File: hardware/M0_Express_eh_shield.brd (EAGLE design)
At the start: 51.3 x 53.3 mm, 30 parts, among them U1 TLV3691, U2 AB0815, U3 Value, U4 MIC841, U5 TPS781, X2 ABS05-32.768KHZ-9-T

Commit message: updates and programmer
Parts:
- removed JP11: (no value), SparkFun-Connectors:1X06-1.27MM
- added JP2: (no value), SparkFun-Connectors:2X5_1.27MM
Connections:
- net GND: now also JP2.10, JP2.9; no longer JP11.1
- net MSP430_RST: now also JP2.5, JP2.6; no longer JP11.3
- net MSP430_TEST: now also JP2.3, JP2.4; no longer JP11.2
- net RX_DEBUG: now also JP2.2; no longer JP11.4
- net TX_DEBUG: now also JP2.7, JP2.8; no longer JP11.5
- net VCC: now also JP2.1; no longer JP11.6

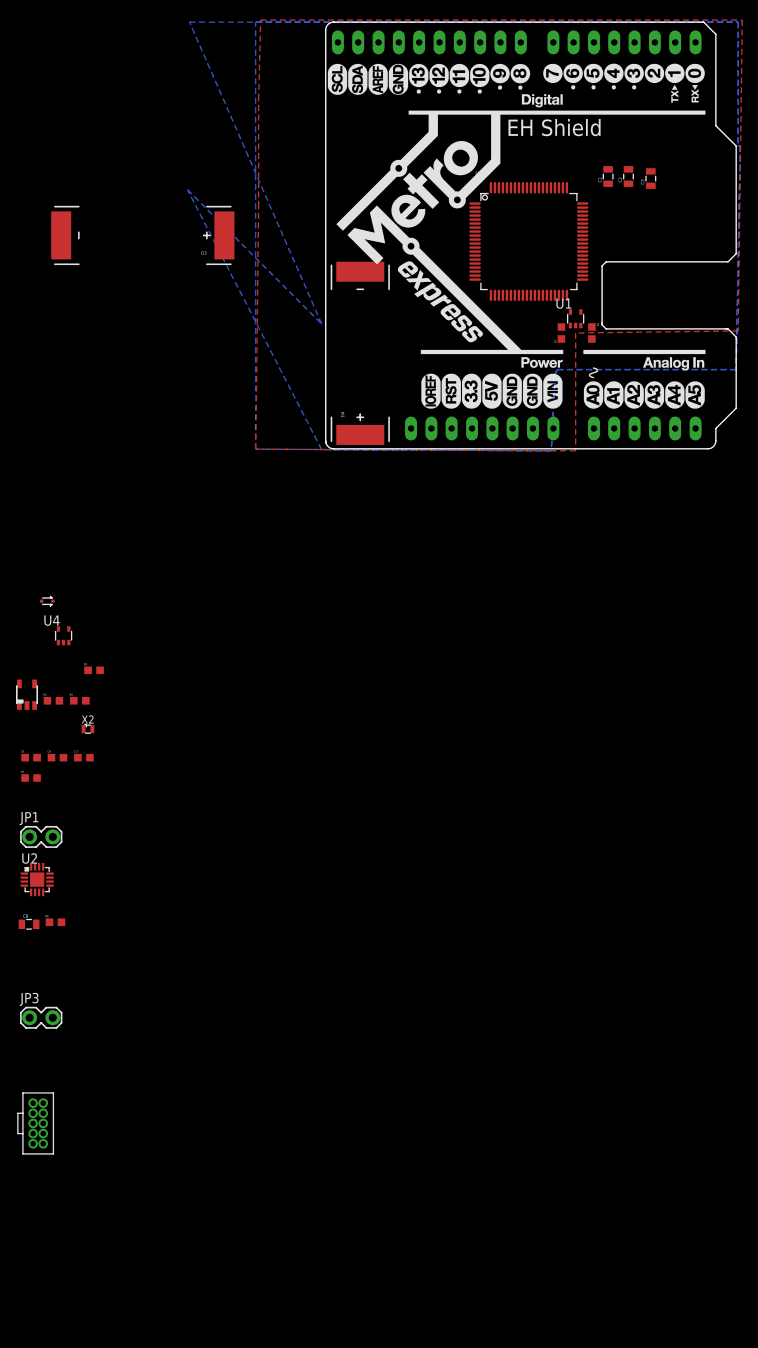
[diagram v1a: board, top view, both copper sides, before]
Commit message: finished schematic, basic board layout, need to route and order
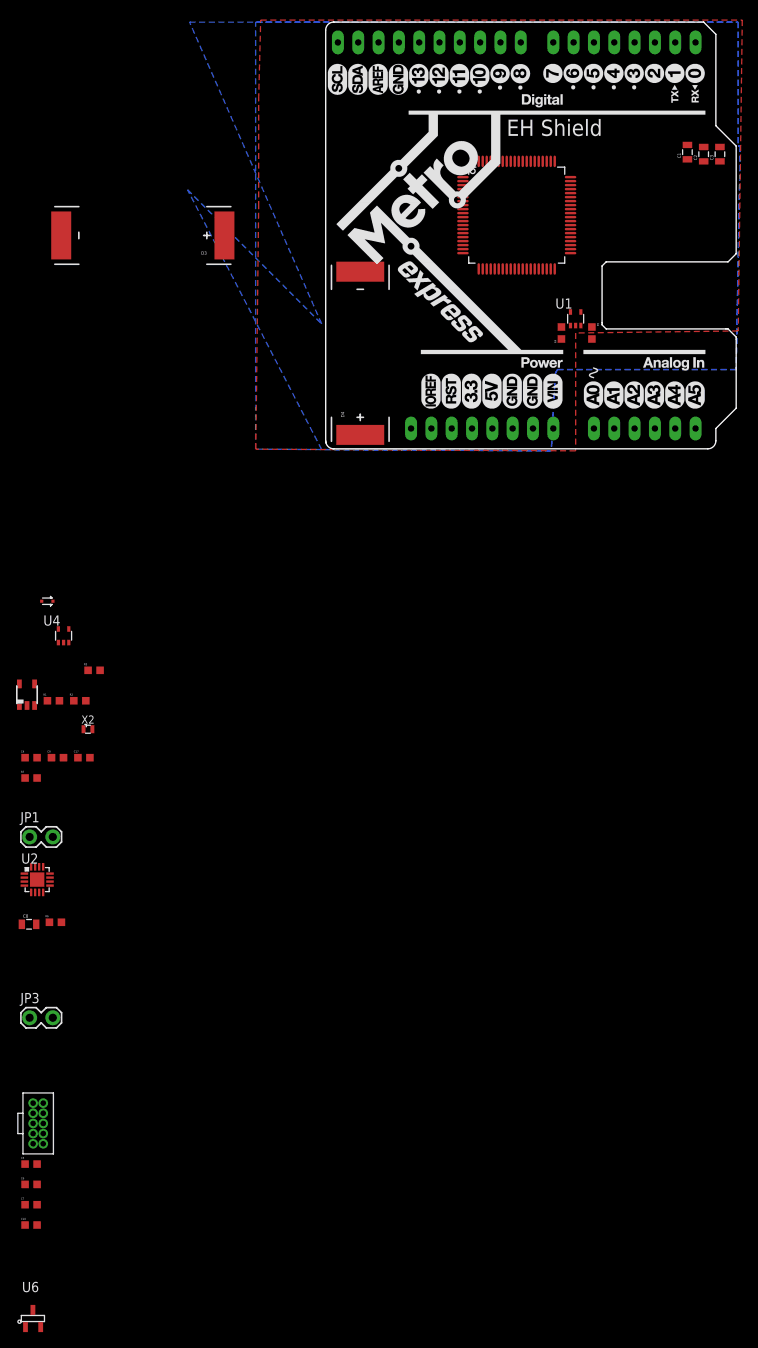
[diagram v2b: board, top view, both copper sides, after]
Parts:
- added C10, C5, C6, C7: 0.1u, tiny_passives:0603
- added U6: ISL21080, isl21080:SOT-23
- R1: value 2.2M -> 695k
- R2: value 2.2M -> 617k
- R3: value 1.3M -> 688k
- R4: value 1.05M -> 2.2M
- R5: value 649k -> 2.9M
- moved R2 78.8 mm to (-13.5, -31.5), turned to 0 degrees
- moved R5 78.8 mm to (50.5, 14.5), turned to 270 degrees
- moved R1 78.4 mm to (-16.8, -31.5), turned to 0 degrees
- moved R4 78.4 mm to (46.7, 14.5), turned to 90 degrees
- moved C1 10.4 mm to (62.5, 37.1)
- moved C2 9.80 mm to (64.5, 36.8)
- moved C3 9.16 mm to (66.5, 36.8)
- moved U3 3.64 mm to (41.1, 29.2)
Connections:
- removed net A4: AD.5
- removed net A5: AD.6
- new net VREF: U1.3, U6.2
- net GND: now also C10.2, C5.2, C6.2, C7.2, R5.1, U6.3; no longer R2.1, U1.3
- net N$2: now also R1.1, R2.1; no longer R4.1, R5.1
- net N$3: now also R2.2; no longer R5.2
- net N$7: now also C6.1
- net PFAIL: now also AD.5
- net VCAP_HALF: now also AD.6, R4.1, R5.2; no longer R1.1, R2.2
- net VCC: now also C10.1, C5.1, C7.1, U6.1

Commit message: finished hardware
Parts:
- removed C1, C3: (no value), SparkFun-Capacitors:0805
- added C11: 0.1u, tiny_passives:0603
- added JP4: (no value), SparkFun-Connectors:SCREWTERMINAL-5MM-2
- C2: value (none) -> 10u
- D1: value RB751 -> BAT20JFILM; device SparkFun-DiscreteSemi:SOD-523 -> SparkFun-DiscreteSemi:SOD-323
- moved U6 154.6 mm to (14.7, 42.1), turned to 90 degrees
- moved C10 144.7 mm to (25.8, 40.3), turned to 270 degrees
- moved C6 143.1 mm to (31.0, 41.9), turned to 90 degrees
- moved JP3 129.0 mm to (44.5, 40.9), turned to 90 degrees
- moved C5 128.9 mm to (3.81, 37.3), turned to 180 degrees
- moved C7 123.9 mm to (18.6, 23.4), turned to 270 degrees
- moved JP2 118.9 mm to (24.6, 28.8), turned to 180 degrees
- moved JP1 111.6 mm to (47.2, 40.9), turned to 90 degrees
- moved R7 89.7 mm to (22.3, 38.3), turned to 90 degrees
- moved R2 89.6 mm to (34.8, 43.9)
- moved R1 88.4 mm to (32.5, 41.9), turned to 270 degrees
- moved D1 88.3 mm to (41.4, 46.7)
- moved C4 88.3 mm to (24.0, 38.2), turned to 90 degrees
- moved U5 87.5 mm to (28.1, 42.3)
- moved R3 86.0 mm to (37.3, 42.9), turned to 90 degrees
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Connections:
- removed net D6: IOL.2
- removed net D7: IOL.1
- net GND: now also C11.2, JP4.2; no longer C1.2, C3.2
- net NV_READ: now also IOL.1, U3.51; no longer IOH.10, U3.52
- net NV_WRITE: now also U3.52; no longer U3.51
- net PFAIL: now also IOL.2, U3.41; no longer AD.5, U3.2
- net REG_SET: now also U3.50; no longer U3.3
- net RTC_CE: now also U3.7; no longer U3.26
- net RTC_SCLK: now also U3.10; no longer U3.25
- net RTC_SIMO: now also U3.8; no longer U3.13
- net RTC_SOMI: now also U3.9; no longer U3.14
- net RX_DEBUG: now also U3.36; no longer U3.42
- net TX_DEBUG: now also U3.35; no longer U3.41
- net VCAP: now also JP4.1; no longer C1.1, C3.1
- net VCAP_HALF: now also IOH.10, U3.27; no longer AD.6, U3.1
- net VCC: now also C11.1
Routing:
- net VCAP: track 0.00 -> 62.9 mm, vias 0 -> 2
- net PFAIL: track 0.00 -> 30.7 mm, vias 0 -> 1
- net VCAP_HALF: track 0.00 -> 28.8 mm, vias 0 -> 2
- net NV_READ: track 0.00 -> 26.5 mm, vias 0 -> 1
- net REG_SET: track 0.00 -> 23.7 mm, vias 0 -> 2
- net VCC: track 0.00 -> 21.7 mm, vias 0 -> 8
- net NV_WRITE: track 0.00 -> 20.3 mm
- net NV_CS: track 0.00 -> 20.3 mm, vias 0 -> 1
- net NV_SIMO: track 0.00 -> 15.9 mm
- net N$10: track 0.00 -> 15.1 mm
- net NV_SOMI: track 0.00 -> 14.6 mm
- net NV_CLK: track 0.00 -> 13.8 mm
- net MSP430_RST: track 0.00 -> 13.3 mm
- net TX_DEBUG: track 0.00 -> 10.4 mm, vias 0 -> 1
- net N$7: track 0.00 -> 10.3 mm
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- added copper zone on layer 16, net VCC
- removed copper zone on layer 16, net GND
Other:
- outline, holes or cut-outs redrawn
- board text added: "+"
- board text added: "CLK"
- board text added: "CP/2"
- board text added: "CS"
- board text added: "Cnct Solar"
- board text added: "EX Cap"
- board text added: "Ext Harv"
- board text added: "PF"
- board text added: "RD"
- board text added: "SIMO"
- board text added: "SOMI"
- board text added: "WR"
- board text added: "_"
- board text removed: "EH Shield"

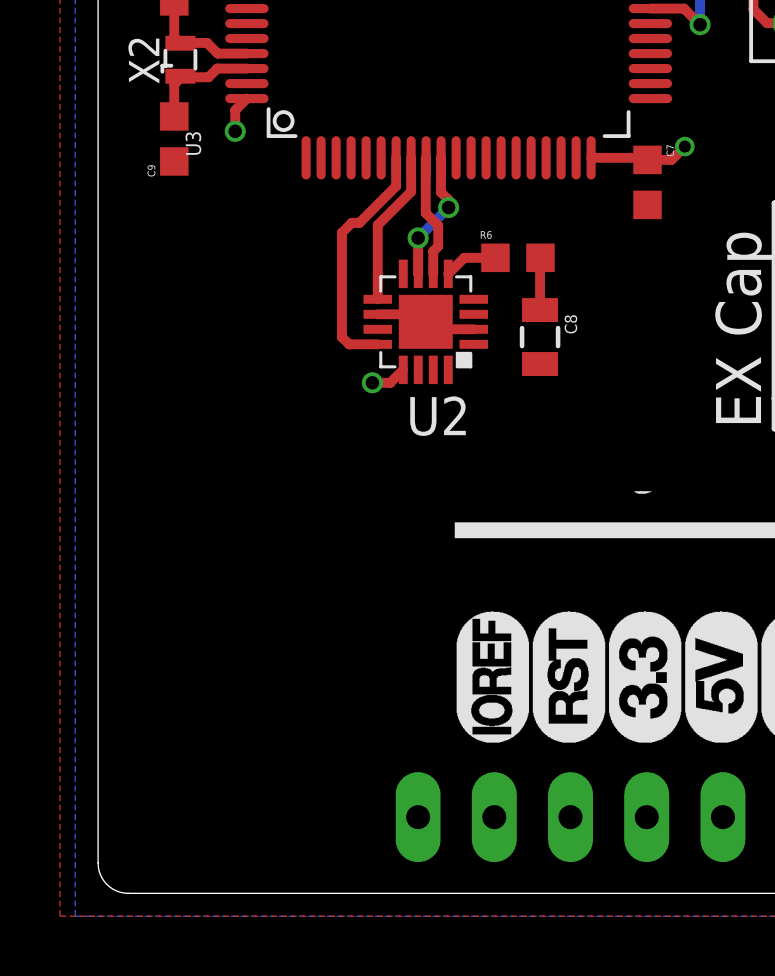
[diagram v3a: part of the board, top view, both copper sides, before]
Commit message: updated with parts and final silk
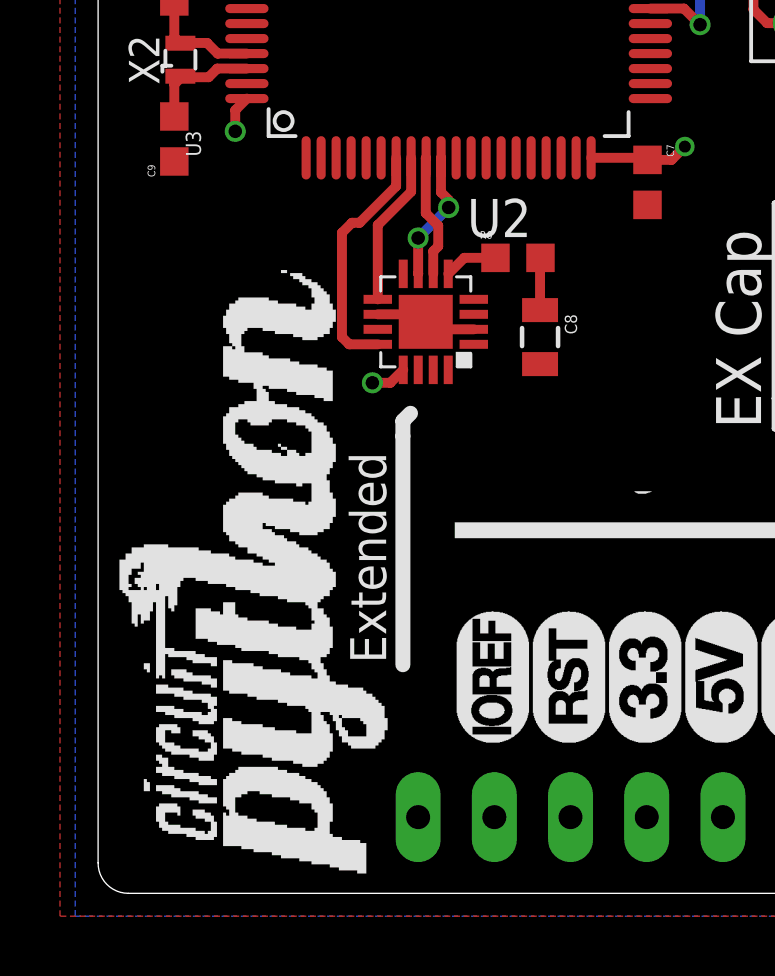
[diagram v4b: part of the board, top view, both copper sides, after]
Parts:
- added U$1: LOGO, circuitpython-logo:CIRCUITPYTHON-LOGO
- R1: value 695k -> 698k
- R2: value 617k -> 619k
- R3: value 688k -> 681k
- R5: value 2.9M -> 2.87M
- renumbered AD to JP_AD, IOH to JP_IOH, IOL to JP_IOL, POWER to JP_POWER
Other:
- board text added: "EH Shield Rev A. for CircuitPython Design: Josiah Hester"
- board text added: "Extended"
- board text removed: "EH Shield for CircuitPython Rev A. Designed by Josiah Hester"
